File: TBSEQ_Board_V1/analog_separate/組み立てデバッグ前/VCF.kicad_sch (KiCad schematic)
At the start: 67 parts, among them J3 Conn_01x02_Pin, Q10 PNP, Q11 NPN, Q12 HN1C01FU-GR,LF_6P DIP, Q13 NPN, Q14 NPN, Q15 NPN, Q16 NPN, Q17 NPN, Q18 NPN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

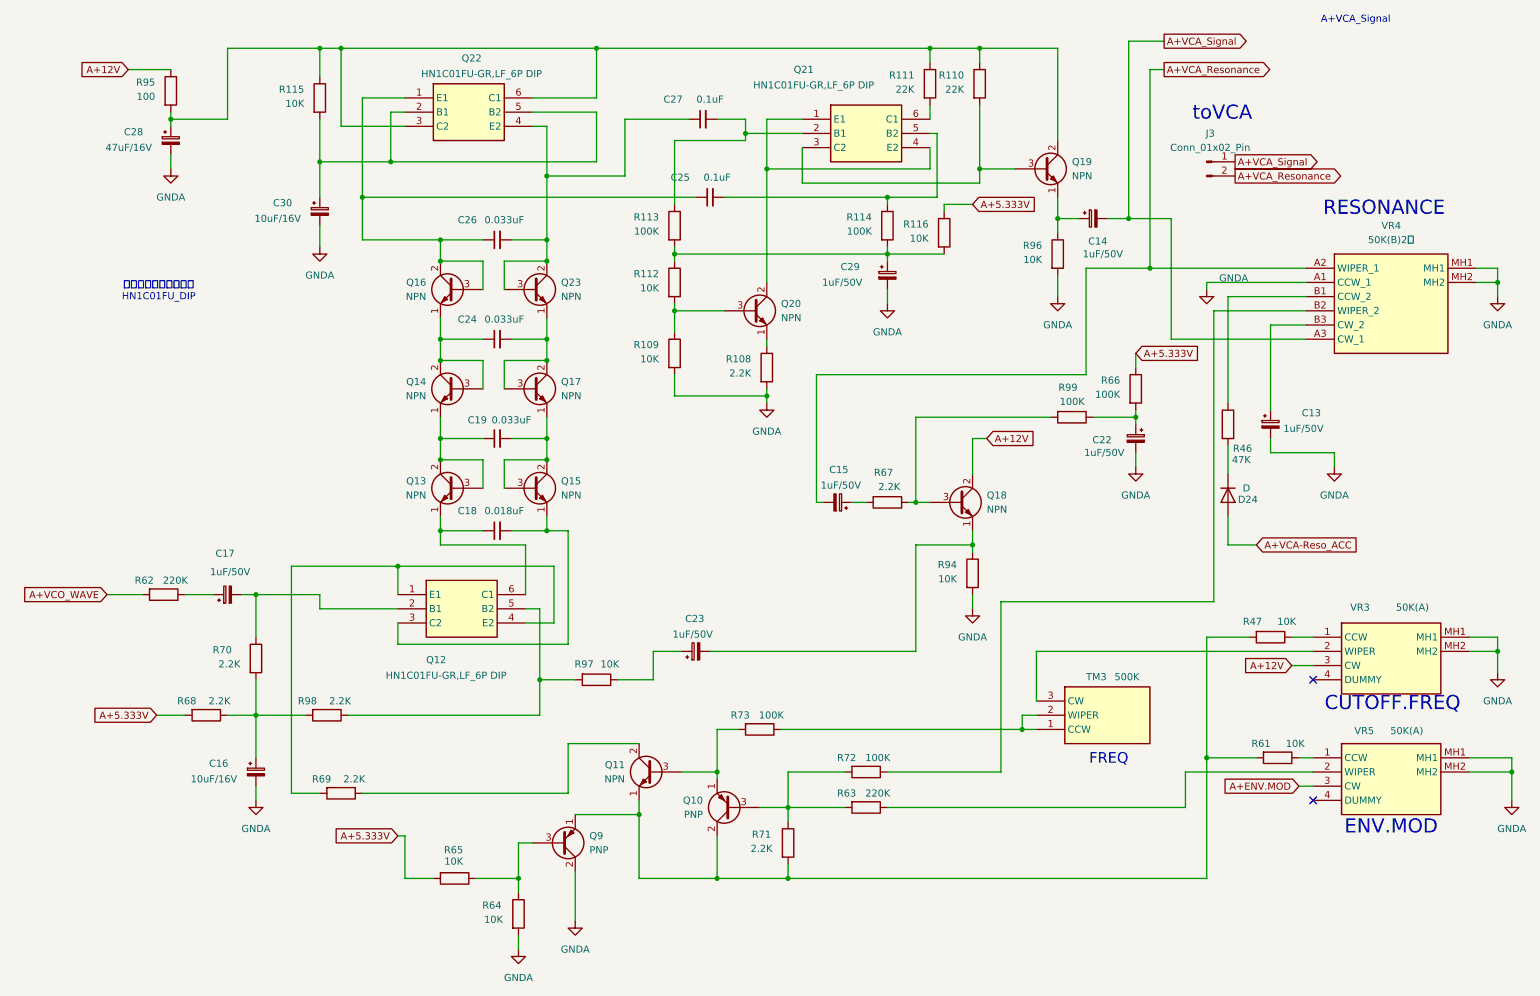
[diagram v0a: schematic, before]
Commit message: analog_separate fix
実装してバグを修正
・VR6以外のボリュームの左右が逆なのを修正
・デュアルトランジスタをHN1C01FU-GRに変更
・VCA CA3080後の出力段のバイアス/増幅率等の設計ミスを修正
・入力信号のシルク位置が間違っているので修正
⇒それ以外は正常動作を確認済
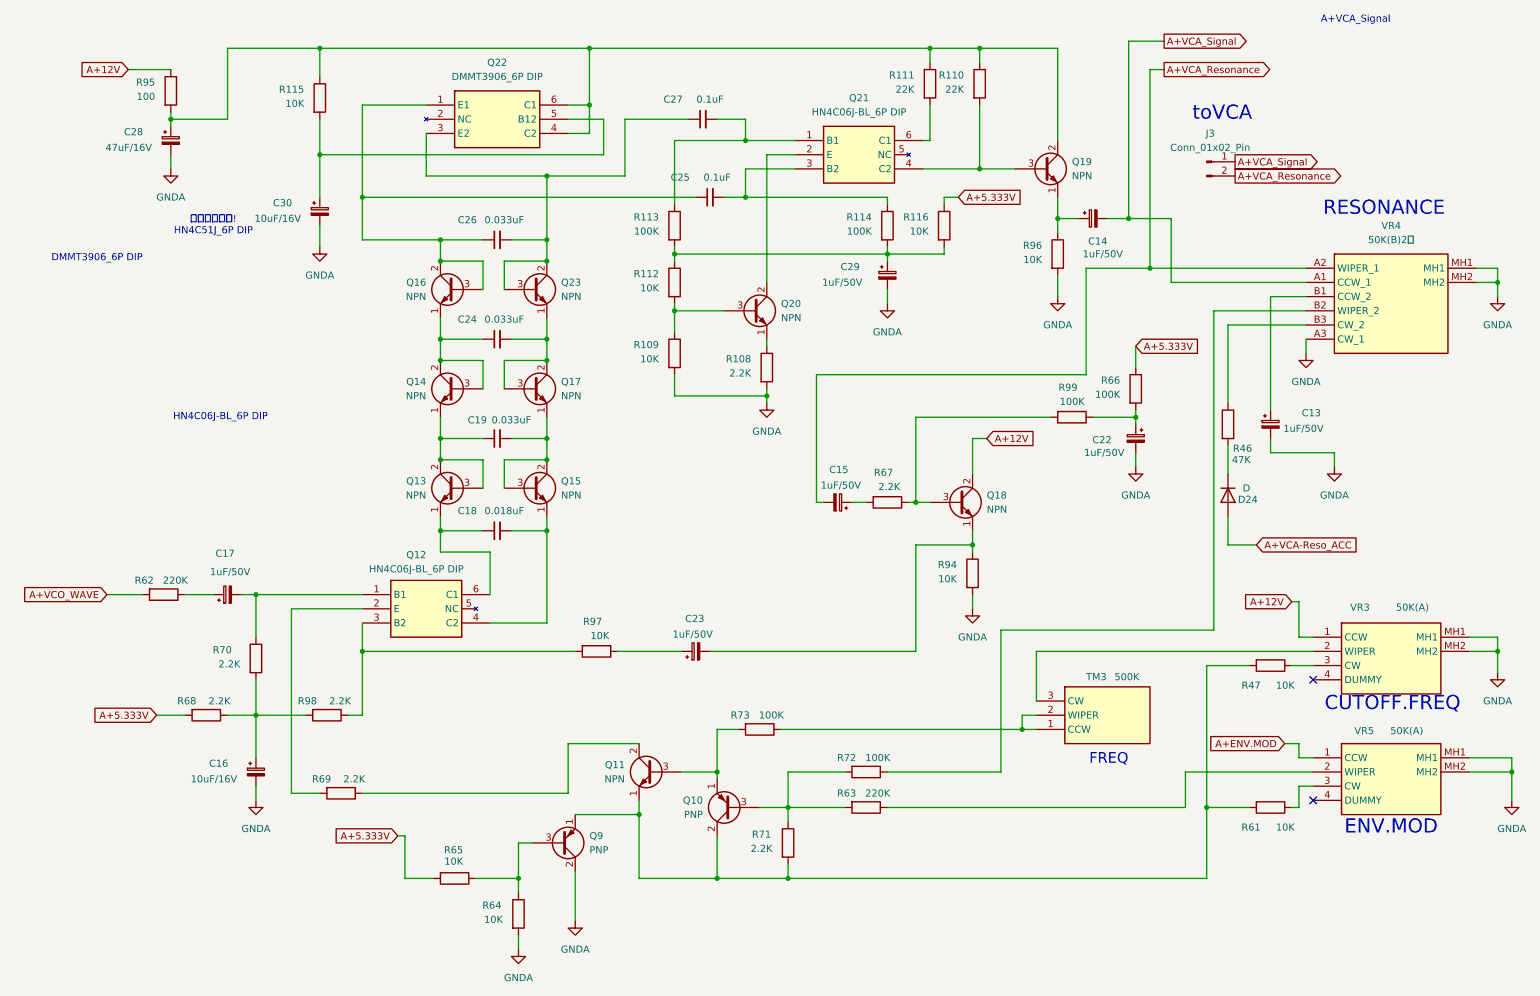
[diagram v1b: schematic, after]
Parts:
- removed Q12, Q21, Q22: HN1C01FU-GR,LF_6P DIP, Package_DIP:DIP-6_W7.62mm, symbol SamacSys_Parts:HN1C01FU-GR,LF_6P DIP変換基板_1
- added Q12, Q21: HN4C06J-BL_6P DIP, Package_DIP:DIP-6_W7.62mm, symbol SamacSys_Parts:HN4C06J-BL_6P DIP変換基板
- added Q22: DMMT3906_6P DIP, Package_DIP:DIP-6_W7.62mm, symbol SamacSys_Parts:DMMT3906-7-F
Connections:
- net A+12V: now also VR3.1 (CCW); no longer VR3.3 (CW)
- net A+ENV.MOD: now also VR5.1 (CCW); no longer VR5.3 (CW)
- net A+VCA_Signal: now also VR4.A1 (CCW_1); no longer VR4.A3 (CW_1)
- net GNDA: now also VR4.A3 (CW_1); no longer VR4.A1 (CCW_1)
- net at C28.1, Q19.2 (C), R110.1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: now also Q22.4 (C2), Q22.6 (C1)
- net at Q19.3 (B), R110.2: now also Q21.4 (C2)
- net at C30.1, R115.2: now also Q22.5 (B12)
- net at R47.1: now also VR3.3 (CW); no longer VR3.1 (CCW)
- net at C13.1: now also VR4.B1 (CCW_2); no longer VR4.B3 (CW_2)
- net at C25.1, C26.1, Q16.2 (C)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: now also Q22.1 (E1)
- net at C26.2, C27.1, Q23.2 (C)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: now also Q22.3 (E2)
- net at R69.2: now also Q12.2 (E)
- net at R111.2: now also Q21.6 (C1)
- net at C18.2, Q15.1 (E): now also Q12.4 (C2)
- net at C25.2, R114.1: now also Q21.3 (B2)
- net at C17.2, R70.1: now also Q12.1 (B1)
- net at R97.2, R98.1: now also Q12.3 (B2)
- net at C18.1, Q13.1 (E): now also Q12.6 (C1)
- net at R46.1: now also VR4.B3 (CW_2); no longer VR4.B1 (CCW_2)
- net at Q20.2 (C): now also Q21.2 (E)
- net at C27.2, R113.1: now also Q21.1 (B1)
- net at R61.1: now also VR5.3 (CW); no longer VR5.1 (CCW)
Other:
- note added: "DMMT3906_6P DIP"
- note added: "HN4C06J-BL_6P DIP"
- note added: "こっちが正解! HN4C51J_6P DIP"
- note removed: "最終的にはこれに統一 HN1C01FU_DIP"
- moved on the sheet: R116, R47, R61, R97
